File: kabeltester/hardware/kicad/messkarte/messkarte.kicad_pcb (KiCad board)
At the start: 4 copper layers, 120 x 90 mm, 112 parts, among them J1 USB-C 5V, J2 Kanalkarte A, J3 Kanalkarte B, J4 Display UART, J5 Display 5V, J6 LED-Streifen, J7 Start-Taster, J8 Fussschalter, Q1 AO3400A, Q2 AO3400A, Q3 AO3400A, Q4 DMN3404L, U1 Raspberry Pi Pico 2, U10 TMUX1101DBVR, U11 TMUX1101DBVR, U12 TMUX1101DBVR, U13 TMUX1101DBVR, U14 ADS1220IPWR, U15 OPA2388IDR, U2 SN74HC595PW, U3 SN74HC595PW, U4 REF5025AIDR, U5 OPA2388IDR, U6 ADG1408YRUZ, U7 ADG1408YRUZ, U8 TMUX1101DBVR, U9 TMUX1101DBVR

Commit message: Zwischenstand: Messkarte/Kanalkarte während des Routings (wird ersetzt)
Co-Authored-By: Claude Opus 5.5 <noreply@anthropic.com>
Claude-Session: https://claude.ai/code/session_0119zGeGQCWTR3UwpEi96iWe
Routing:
- removed copper zone on In2.Cu, net 5VA
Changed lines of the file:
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@@
   (layers
     (0 "F.Cu" signal)
-    (1 "In1.Cu" signal)
+    (1 "In1.Cu" power)
     (2 "In2.Cu" signal)
     (31 "B.Cu" signal)
@@
   )
   (zone (net 15) (net_name "GND") (layer "In1.Cu") (hatch edge 0.5)
-    (connect_pads (clearance 0.25))
-    (min_thickness 0.2) (filled_areas_thickness no)
-    (fill yes (thermal_gap 0.3) (thermal_bridge_width 0.35))
-    (polygon
-      (pts
-        (xy 0.4 0.4)
-        (xy 119.6 0.4)
-        (xy 119.6 89.6)
-        (xy 0.4 89.6)
-      )
-    )
-  )
-  (zone (net 3) (net_name "5VA") (layer "In2.Cu") (hatch edge 0.5)
-    (connect_pads (clearance 0.25))
+    (connect_pads yes (clearance 0.2))
     (min_thickness 0.2) (filled_areas_thickness no)
     (fill yes (thermal_gap 0.3) (thermal_bridge_width 0.35))
@@
   )
   (zone (net 15) (net_name "GND") (layer "B.Cu") (hatch edge 0.5)
-    (connect_pads (clearance 0.25))
+    (connect_pads yes (clearance 0.2))
     (min_thickness 0.2) (filled_areas_thickness no)
     (fill yes (thermal_gap 0.3) (thermal_bridge_width 0.35))

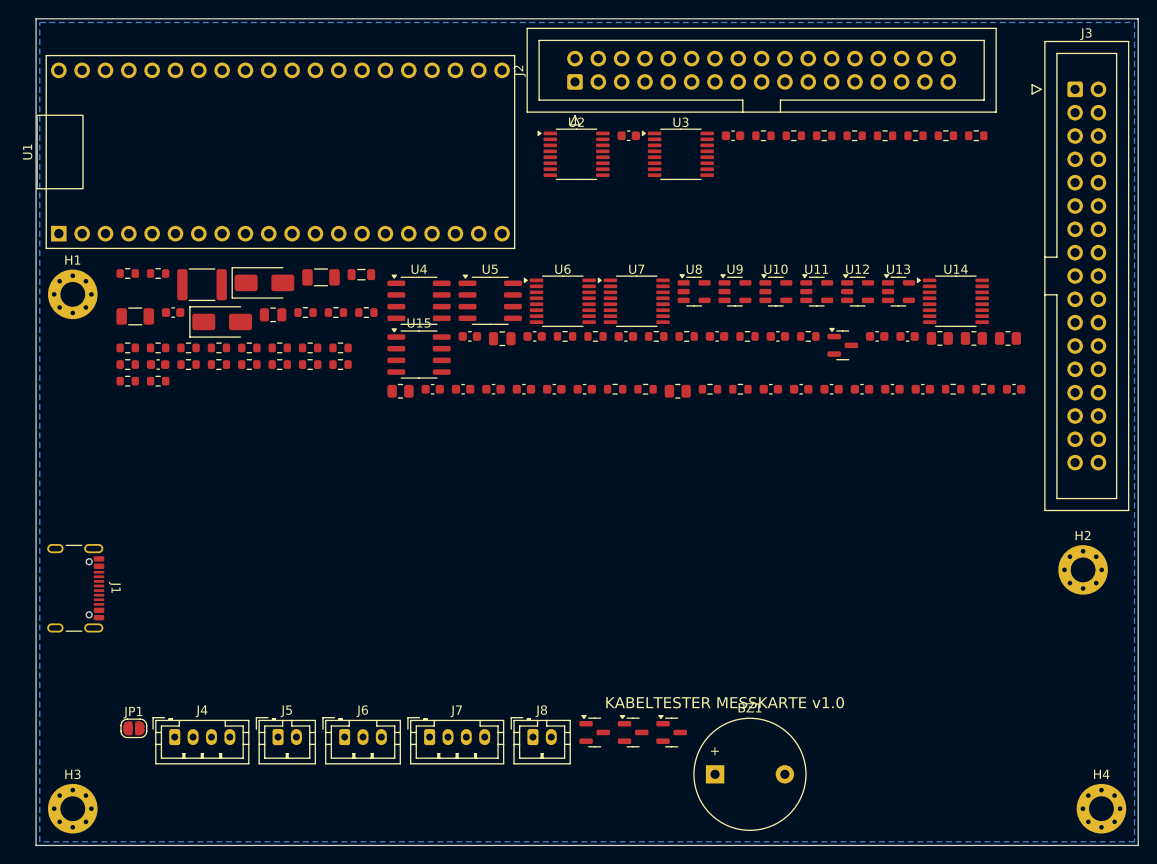
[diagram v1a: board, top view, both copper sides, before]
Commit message: Routing: Adapter vollständig (DRC 0), Messkarte bis auf 17 Verbindungen
- Adapter 2x RJ45: 0 DRC-Fehler, 0 offene Verbindungen, 174 Masse-Vias
- Messkarte: 297 -> 17 offen (13 kleine GND-Inseln ohne Via-Platz, 4 Signalnetze)
- Generator: Masse-Fanout für unverbundene GND-Pads, Via je Masseinsel, GND-Fläche oben

Co-Authored-By: Claude Opus 5.5 <noreply@anthropic.com>
Claude-Session: https://claude.ai/code/session_0119zGeGQCWTR3UwpEi96iWe
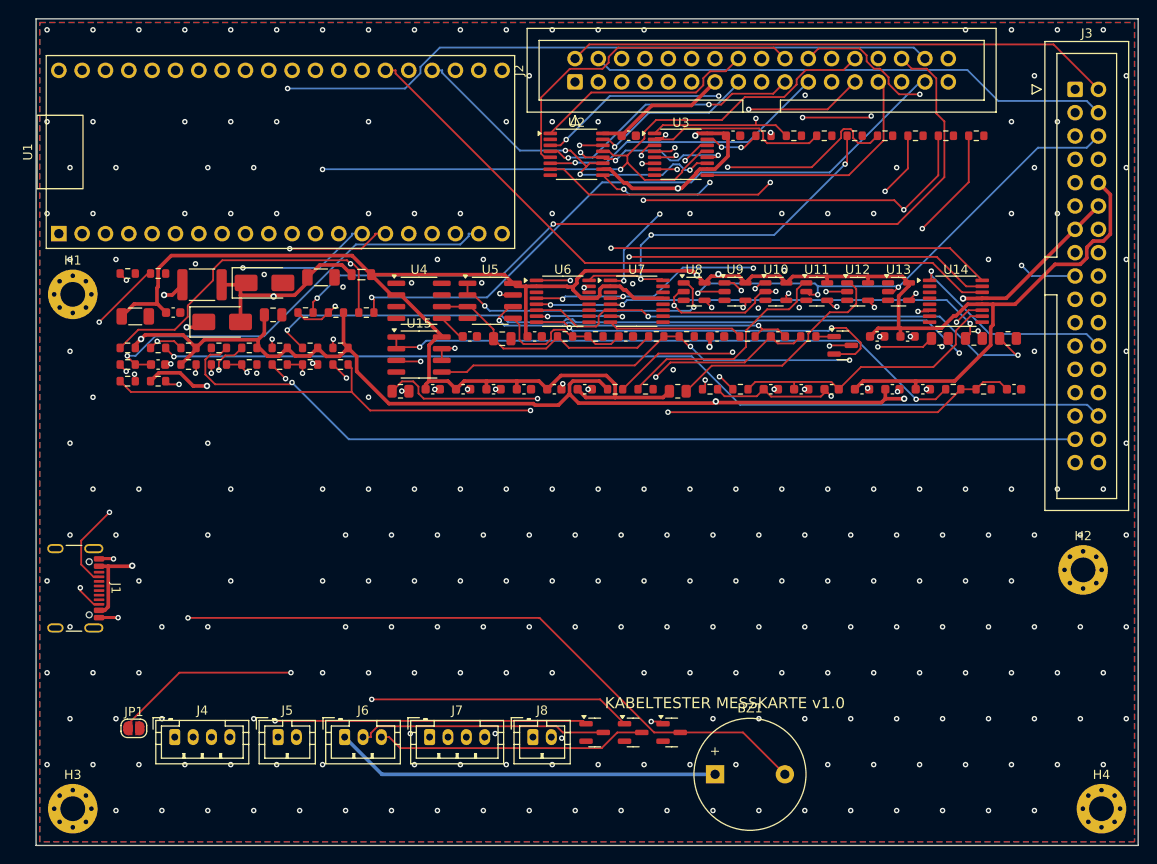
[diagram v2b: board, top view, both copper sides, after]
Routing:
- net 5VA: track 0.00 -> 278.4 mm, vias 0 -> 3
- net 3V3: track 0.00 -> 245.1 mm, vias 0 -> 6
- net SR_OE_N: track 0.00 -> 165.0 mm, vias 0 -> 3
- net LO_S: track 0.00 -> 139.2 mm, vias 0 -> 2
- net +5V: track 0.00 -> 135.9 mm, vias 0 -> 2
- net HI_F: track 0.00 -> 114.5 mm, vias 0 -> 3
- net SR_CLK: track 0.00 -> 109.9 mm, vias 0 -> 4
- net ADAPT_B_N: track 0.00 -> 109.0 mm, vias 0 -> 2
- net SR_LATCH: track 0.00 -> 105.9 mm, vias 0 -> 4
- net SDA_XB: track 0.00 -> 104.7 mm, vias 0 -> 1
- net HI_S: track 0.00 -> 104.2 mm, vias 0 -> 1
- net ADAPT_A_N: track 0.00 -> 103.5 mm, vias 0 -> 2
- net SCL_XB: track 0.00 -> 102.2 mm, vias 0 -> 1
- net SCAN_ADC: track 0.00 -> 100.9 mm, vias 0 -> 1
- net BZ_K: track 0.00 -> 99.5 mm, vias 0 -> 2
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- added copper zone on F.Cu, net GND
